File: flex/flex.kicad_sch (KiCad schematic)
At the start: 105 parts, among them J1 Conn_01x06_Female, J2 Conn_01x05_Female, J3 Conn_01x06_Female, J4 Conn_01x03_Female, J5 Conn_01x03_Female, SW1 SW_Push, SW10 SW_Push, SW11 SW_Push, SW12 SW_Push, SW13 SW_Push, SW14 SW_Push, SW15 SW_Push, SW16 SW_Push, SW17 SW_Push, SW18 SW_Push, SW19 SW_Push, SW2 SW_Push, SW20 SW_Push, SW21 SW_Push, SW22 SW_Push, SW23 SW_Push, SW24 SW_Push, SW3 SW_Push, SW4 SW_Push, SW5 SW_Push, SW6 SW_Push, SW7 SW_Push, SW8 SW_Push, SW9 SW_Push

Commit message: footprints
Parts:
- D1, D10, D11, D12, D2, D25, D26, D27, D28, D29, D3, D30, D31, D32, D33, D34, D35, D36, D4, D5, D6, D7, D8, D9: footprint libs:D_0402 -> libs:D_SOD-523
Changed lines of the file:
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@@
       (effects (font (size 1.27 1.27)) (justify right))
     )
-    (property "Footprint" "libs:D_0402" (at 66.04 44.45 0)
+    (property "Footprint" "libs:D_SOD-523" (at 66.04 44.45 0)
       (effects (font (size 1.27 1.27)) hide)
     )
@@
       (effects (font (size 1.27 1.27)) (justify right))
     )
-    (property "Footprint" "libs:D_0402" (at 226.06 57.15 0)
+    (property "Footprint" "libs:D_SOD-523" (at 226.06 57.15 0)
       (effects (font (size 1.27 1.27)) hide)
     )
@@
       (effects (font (size 1.27 1.27)) (justify right))
     )
-    (property "Footprint" "libs:D_0402" (at 226.06 80.01 0)
+    (property "Footprint" "libs:D_SOD-523" (at 226.06 80.01 0)
       (effects (font (size 1.27 1.27)) hide)
     )
@@
       (effects (font (size 1.27 1.27)) (justify right))
     )
-    (property "Footprint" "libs:D_0402" (at 330.2 57.15 0)
+    (property "Footprint" "libs:D_SOD-523" (at 330.2 57.15 0)
       (effects (font (size 1.27 1.27)) hide)
     )
@@
       (effects (font (size 1.27 1.27)) (justify right))
     )
-    (property "Footprint" "libs:D_0402" (at 176.53 80.01 0)
+    (property "Footprint" "libs:D_SOD-523" (at 176.53 80.01 0)
       (effects (font (size 1.27 1.27)) hide)
     )
@@
       (effects (font (size 1.27 1.27)) (justify right))
     )
-    (property "Footprint" "libs:D_0402" (at 176.53 57.15 0)
+    (property "Footprint" "libs:D_SOD-523" (at 176.53 57.15 0)
       (effects (font (size 1.27 1.27)) hide)
     )
@@
       (effects (font (size 1.27 1.27)) (justify right))
     )
-    (property "Footprint" "libs:D_0402" (at 279.4 93.98 0)
+    (property "Footprint" "libs:D_SOD-523" (at 279.4 93.98 0)
       (effects (font (size 1.27 1.27)) hide)
     )
@@
       (effects (font (size 1.27 1.27)) (justify right))
     )
-    (property "Footprint" "libs:D_0402" (at 118.11 93.98 0)
+    (property "Footprint" "libs:D_SOD-523" (at 118.11 93.98 0)
       (effects (font (size 1.27 1.27)) hide)
     )
@@
       (effects (font (size 1.27 1.27)) (justify right))
     )
-    (property "Footprint" "libs:D_0402" (at 276.86 57.15 0)
+    (property "Footprint" "libs:D_SOD-523" (at 276.86 57.15 0)
       (effects (font (size 1.27 1.27)) hide)
     )
@@
       (effects (font (size 1.27 1.27)) (justify right))
     )
-    (property "Footprint" "libs:D_0402" (at 66.04 93.98 0)
+    (property "Footprint" "libs:D_SOD-523" (at 66.04 93.98 0)
       (effects (font (size 1.27 1.27)) hide)
     )
@@
       (effects (font (size 1.27 1.27)) (justify right))
     )
-    (property "Footprint" "libs:D_0402" (at 116.84 44.45 0)
+    (property "Footprint" "libs:D_SOD-523" (at 116.84 44.45 0)
       (effects (font (size 1.27 1.27)) hide)
     )
@@
       (effects (font (size 1.27 1.27)) (justify right))
     )
-    (property "Footprint" "libs:D_0402" (at 226.06 93.98 0)
+    (property "Footprint" "libs:D_SOD-523" (at 226.06 93.98 0)
       (effects (font (size 1.27 1.27)) hide)
     )
@@
       (effects (font (size 1.27 1.27)) (justify right))
     )
-    (property "Footprint" "libs:D_0402" (at 226.06 43.18 0)
+    (property "Footprint" "libs:D_SOD-523" (at 226.06 43.18 0)
       (effects (font (size 1.27 1.27)) hide)
     )
@@
       (effects (font (size 1.27 1.27)) (justify right))
     )
-    (property "Footprint" "libs:D_0402" (at 330.2 80.01 0)
+    (property "Footprint" "libs:D_SOD-523" (at 330.2 80.01 0)
       (effects (font (size 1.27 1.27)) hide)
     )
@@
       (effects (font (size 1.27 1.27)) (justify right))
     )
-    (property "Footprint" "libs:D_0402" (at 279.4 80.01 0)
+    (property "Footprint" "libs:D_SOD-523" (at 279.4 80.01 0)
       (effects (font (size 1.27 1.27)) hide)
     )
@@
       (effects (font (size 1.27 1.27)) (justify right))
     )
-    (property "Footprint" "libs:D_0402" (at 116.84 58.42 0)
+    (property "Footprint" "libs:D_SOD-523" (at 116.84 58.42 0)
       (effects (font (size 1.27 1.27)) hide)
     )
@@
       (effects (font (size 1.27 1.27)) (justify right))
     )
-    (property "Footprint" "libs:D_0402" (at 118.11 80.01 0)
+    (property "Footprint" "libs:D_SOD-523" (at 118.11 80.01 0)
       (effects (font (size 1.27 1.27)) hide)
     )
@@
       (effects (font (size 1.27 1.27)) (justify right))
     )
-    (property "Footprint" "libs:D_0402" (at 176.53 43.18 0)
+    (property "Footprint" "libs:D_SOD-523" (at 176.53 43.18 0)
       (effects (font (size 1.27 1.27)) hide)
     )
@@
       (effects (font (size 1.27 1.27)) (justify right))
     )
-    (property "Footprint" "libs:D_0402" (at 330.2 43.18 0)
+    (property "Footprint" "libs:D_SOD-523" (at 330.2 43.18 0)
       (effects (font (size 1.27 1.27)) hide)
     )
@@
       (effects (font (size 1.27 1.27)) (justify right))
     )
-    (property "Footprint" "libs:D_0402" (at 66.04 80.01 0)
+    (property "Footprint" "libs:D_SOD-523" (at 66.04 80.01 0)
       (effects (font (size 1.27 1.27)) hide)
     )
@@
       (effects (font (size 1.27 1.27)) (justify right))
     )
-    (property "Footprint" "libs:D_0402" (at 330.2 93.98 0)
+    (property "Footprint" "libs:D_SOD-523" (at 330.2 93.98 0)
       (effects (font (size 1.27 1.27)) hide)
     )
@@
       (effects (font (size 1.27 1.27)) (justify right))
     )
-    (property "Footprint" "libs:D_0402" (at 66.04 58.42 0)
+    (property "Footprint" "libs:D_SOD-523" (at 66.04 58.42 0)
       (effects (font (size 1.27 1.27)) hide)
     )
@@
       (effects (font (size 1.27 1.27)) (justify right))
     )
-    (property "Footprint" "libs:D_0402" (at 276.86 43.18 0)
+    (property "Footprint" "libs:D_SOD-523" (at 276.86 43.18 0)
       (effects (font (size 1.27 1.27)) hide)
     )
@@
       (effects (font (size 1.27 1.27)) (justify right))
     )
-    (property "Footprint" "libs:D_0402" (at 176.53 93.98 0)
-      (effects (font (size 1.27 1.27)) hide)
-    )
+    (property "Footprint" "libs:D_SOD-523" (at 176.53 93.98 0)
+      (effects (font (size 1.27 1.27)) hide)
+    )

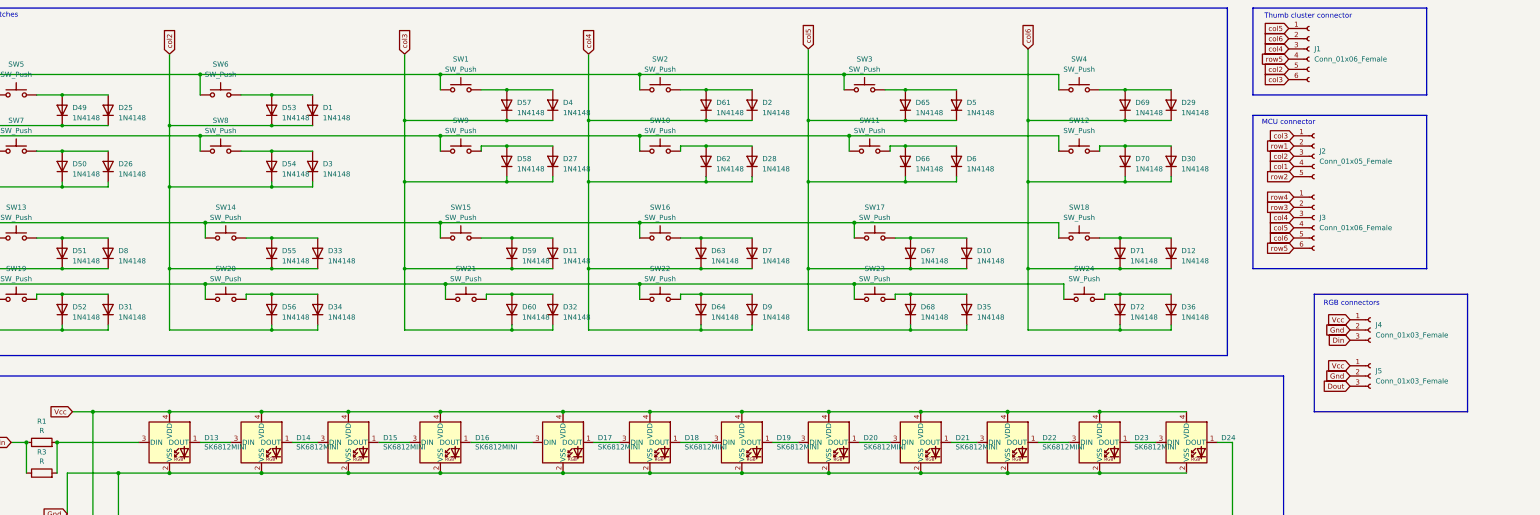
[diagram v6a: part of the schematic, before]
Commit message: separate into right/left diodes
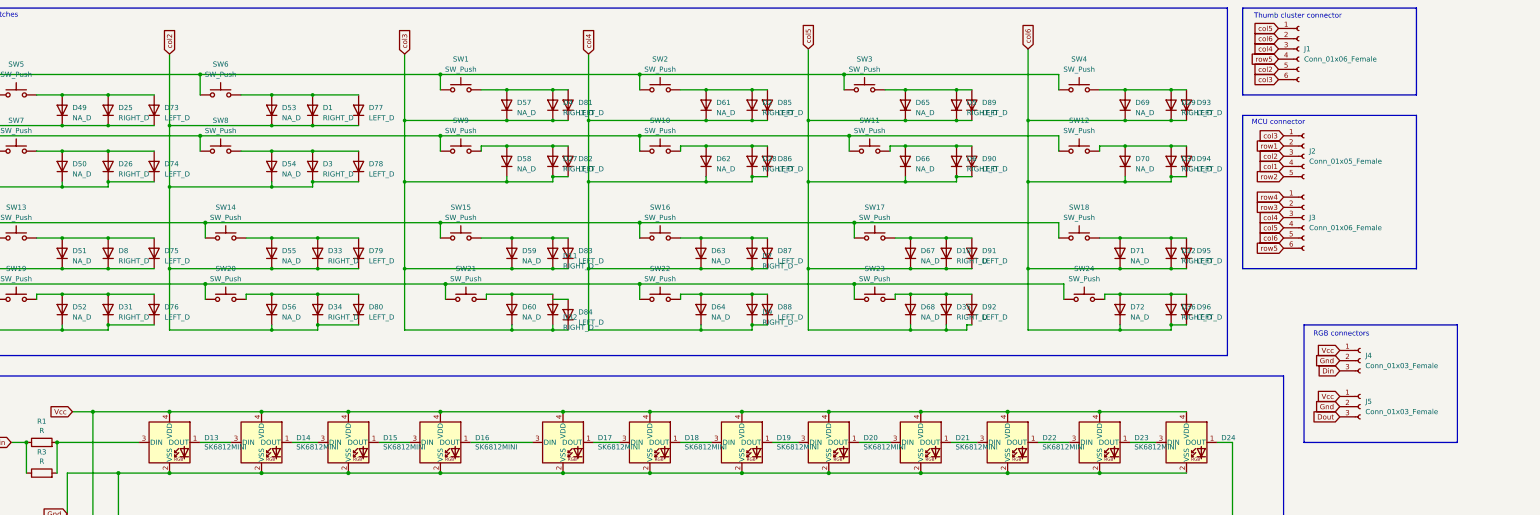
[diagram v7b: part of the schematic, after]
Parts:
- added D73, D74, D75, D76, D77, D78, D79, D80, D81, D82, D83, D84, D85, D86, D87, D88, D89, D90, D91, D92, D93, D94, D95, D96: LEFT_D, libs:D_SOD-523, symbol Diode:1N4148
- D1, D10, D11, D12, D2, D25, D26, D27, D28, D29, D3, D30, D31, D32, D33, D34, D35, D36, D4, D5, D6, D7, D8, D9: value 1N4148 -> RIGHT_D
- D49, D50, D51, D52, D53, D54, D55, D56, D57, D58, D59, D60, D61, D62, D63, D64, D65, D66, D67, D68, D69, D70, D71, D72: value 1N4148 -> NA_D
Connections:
- net col1: now also D73.1 (K), D74.1 (K), D75.1 (K), D76.1 (K)
- net col2: now also D77.1 (K), D78.1 (K), D79.1 (K), D80.1 (K)
- net col3: now also D81.1 (K), D82.1 (K), D83.1 (K), D84.1 (K)
- net col4: now also D85.1 (K), D86.1 (K), D87.1 (K), D88.1 (K)
- net col5: now also D89.1 (K), D90.1 (K), D91.1 (K), D92.1 (K)
- net col6: now also D93.1 (K), D94.1 (K), D95.1 (K), D96.1 (K)
- net at D26.2 (A), D50.2 (A), SW7.2: now also D74.2 (A)
- net at D25.2 (A), D49.2 (A), SW5.2: now also D73.2 (A)
- net at D35.2 (A), D68.2 (A), SW23.2: now also D92.2 (A)
- net at D28.2 (A), D62.2 (A), SW10.2: now also D86.2 (A)
- net at D63.2 (A), D7.2 (A), SW16.2: now also D87.2 (A)
- net at D2.2 (A), D61.2 (A), SW2.2: now also D85.2 (A)
- net at D30.2 (A), D70.2 (A), SW12.2: now also D94.2 (A)
- net at D11.2 (A), D59.2 (A), SW15.2: now also D83.2 (A)
- net at D27.2 (A), D58.2 (A), SW9.2: now also D82.2 (A)
- net at D1.2 (A), D53.2 (A), SW6.2: now also D77.2 (A)
- net at D34.2 (A), D56.2 (A), SW20.2: now also D80.2 (A)
- net at D6.2 (A), D66.2 (A), SW11.2: now also D90.2 (A)
- net at D33.2 (A), D55.2 (A), SW14.2: now also D79.2 (A)
- net at D10.2 (A), D67.2 (A), SW17.2: now also D91.2 (A)
- net at D3.2 (A), D54.2 (A), SW8.2: now also D78.2 (A)
- net at D51.2 (A), D8.2 (A), SW13.2: now also D75.2 (A)
- net at D31.2 (A), D52.2 (A), SW19.2: now also D76.2 (A)
- net at D64.2 (A), D9.2 (A), SW22.2: now also D88.2 (A)
- net at D12.2 (A), D71.2 (A), SW18.2: now also D95.2 (A)
- net at D4.2 (A), D57.2 (A), SW1.2: now also D81.2 (A)
- net at D5.2 (A), D65.2 (A), SW3.2: now also D89.2 (A)
- net at D29.2 (A), D69.2 (A), SW4.2: now also D93.2 (A)
- net at D36.2 (A), D72.2 (A), SW24.2: now also D96.2 (A)
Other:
- moved on the sheet: D10, D35, J1, J2, J3, J4, J5

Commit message: left/right capacitor resistor
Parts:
- added C2: LEFT_C, libs:D_0402, symbol Device:C
- added R2: LEFT_R, libs:D_0402, symbol Device:R
- C1: value C -> RIGHT_C
- C3: value C3 -> NA_C
- J1, J3: value Conn_01x06_Female -> NA_Conn_01x06_Female
- J2: value Conn_01x05_Female -> NA_Conn_01x05_Female
- J4, J5: value Conn_01x03_Female -> NA_Conn_01x03_Female
- R1: value R -> RIGHT_R
- R3: value R -> NA_R
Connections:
- net Din: now also R2.1
- net Gnd: now also C2.2
- net Vcc: now also C2.1
- net at D13.3 (DIN), R1.2, R3.2: now also R2.2
- net at D32.2 (A), D60.2 (A), SW21.2: now also D84.2 (A)
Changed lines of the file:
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@@
   (junction (at 66.04 76.2) (diameter 0) (color 0 0 0 0)
   )
+  (junction (at 176.53 90.17) (diameter 0) (color 0 0 0 0)
+  )
   (junction (at 330.2 53.34) (diameter 0) (color 0 0 0 0)
   )
@@
   (junction (at 176.53 39.37) (diameter 0) (color 0 0 0 0)
   )
+  (junction (at 48.26 182.88) (diameter 0) (color 0 0 0 0)
+  )
   (junction (at 165.1 53.34) (diameter 0) (color 0 0 0 0)
   )
@@
   (junction (at 148.59 134.62) (diameter 1.016) (color 0 0 0 0)
   )
+  (junction (at 45.72 130.81) (diameter 0) (color 0 0 0 0)
+  )
   (junction (at 82.55 166.37) (diameter 1.016) (color 0 0 0 0)
   )
@@
   (junction (at 214.63 46.99) (diameter 0) (color 0 0 0 0)
   )
+  (junction (at 48.26 175.26) (diameter 0) (color 0 0 0 0)
+  )
   (junction (at 245.11 134.62) (diameter 1.016) (color 0 0 0 0)
   )
@@
   (junction (at 127 181.61) (diameter 1.016) (color 0 0 0 0)
   )
+  (junction (at 53.34 130.81) (diameter 0) (color 0 0 0 0)
+  )
   (junction (at 260.35 181.61) (diameter 1.016) (color 0 0 0 0)
   )
@@
     (stroke (width 0) (type solid))
   )
+  (wire (pts (xy 53.34 130.81) (xy 53.34 134.62))
+    (stroke (width 0) (type solid))
+  )
   (wire (pts (xy 81.28 63.5) (xy 81.28 83.82))
     (stroke (width 0) (type solid))
@@
     (stroke (width 0) (type solid))
   )
+  (wire (pts (xy 180.34 91.44) (xy 176.53 91.44))
+    (stroke (width 0) (type default))
+  )
   (wire (pts (xy 198.12 87.63) (xy 198.12 91.44))
     (stroke (width 0) (type solid))
@@
     (stroke (width 0) (type default))
   )
+  (wire (pts (xy 48.26 175.26) (xy 52.07 175.26))
+    (stroke (width 0) (type default))
+  )
   (wire (pts (xy 276.86 60.96) (xy 280.67 60.96))
     (stroke (width 0) (type default))
@@
     (stroke (width 0) (type solid))
   )
-  (wire (pts (xy 45.72 175.26) (xy 52.07 175.26))
+  (wire (pts (xy 45.72 175.26) (xy 48.26 175.26))
     (stroke (width 0) (type default))
   )
@@
     (stroke (width 0) (type solid))
   )
-  (wire (pts (xy 45.72 182.88) (xy 52.07 182.88))
+  (wire (pts (xy 45.72 182.88) (xy 48.26 182.88))
     (stroke (width 0) (type default))
   )
@@
     (stroke (width 0) (type solid))
   )
+  (wire (pts (xy 48.26 182.88) (xy 52.07 182.88))
+    (stroke (width 0) (type default))
+  )
   (wire (pts (xy 35.56 50.8) (xy 38.1 50.8))
     (stroke (width 0) (type solid))
@@
     (stroke (width 0) (type default))
   )
-  (wire (pts (xy 45.72 127) (xy 45.72 134.62))
+  (wire (pts (xy 45.72 127) (xy 45.72 130.81))
     (stroke (width 0) (type default))
   )
@@
     (stroke (width 0) (type solid))
   )
+  (wire (pts (xy 45.72 130.81) (xy 45.72 134.62))
+    (stroke (width 0) (type default))
+  )
   (polyline (pts (xy 347.98 45.72) (xy 347.98 83.82))
     (stroke (width 0) (type default))
@@
     (stroke (width 0) (type solid))
   )
-  (wire (pts (xy 53.34 127) (xy 53.34 134.62))
+  (wire (pts (xy 53.34 127) (xy 53.34 130.81))
     (stroke (width 0) (type solid))
   )
@@
     (stroke (width 0) (type solid))
   )
+  (wire (pts (xy 176.53 91.44) (xy 176.53 90.17))
+    (stroke (width 0) (type default))
+  )
   (wire (pts (xy 171.45 166.37) (xy 193.04 166.37))
     (stroke (width 0) (type solid))
@@
     (stroke (width 0) (type solid))
   )
-  (wire (pts (xy 176.53 91.44) (xy 180.34 91.44))
-    (stroke (width 0) (type solid))
-  )
   (wire (pts (xy 223.52 119.38) (xy 245.11 119.38))
     (stroke (width 0) (type solid))
@@
     )
   )
+  (symbol (lib_id "Device:R") (at 49.53 130.81 90) (unit 1)
+    (in_bom yes) (on_board yes) (dnp no)
+    (property "Reference" "R2" (at 49.53 125.5838 90)
+      (effects (font (size 1.27 1.27)))
+    )
+    (property "Value" "LEFT_R" (at 49.53 127.8825 90)
+      (effects (font (size 1.27 1.27)))
+    )
+    (property "Footprint" "libs:D_0402" (at 49.53 132.588 90)
+      (effects (font (size 1.27 1.27)) hide)
+    )
+    (property "Datasheet" "~" (at 49.53 130.81 0)
+      (effects (font (size 1.27 1.27)) hide)
+    )
+    (pin "1")
+    (pin "2")
+    (instances
+      (project "flex"
+        (path "/e63e39d7-6ac0-4ffd-8aa3-1841a4541b55"
+          (reference "R2") (unit 1)
+        )
+      )
+    )
+  )
   (symbol (lib_id "Device:C") (at 38.1 179.07 0) (unit 1)
     (in_bom yes) (on_board yes) (dnp no)
@@
       (effects (font (size 1.27 1.27)) (justify left))
     )
-    (property "Value" "C" (at 41.0211 180.2193 0)
+    (property "Value" "RIGHT_C" (at 41.0211 180.2193 0)
       (effects (font (size 1.27 1.27)) (justify left))
     )
@@
       (effects (font (size 1.27 1.27)) (justify left))
     )
-    (property "Value" "Conn_01x03_Female" (at 378.46 119.38 0)
+    (property "Value" "NA_Conn_01x03_Female" (at 378.46 119.38 0)
       (effects (font (size 1.27 1.27)) (justify left))
     )
@@
     )
   )
+  (symbol (lib_id "Device:C") (at 48.26 179.07 0) (unit 1)
+    (in_bom yes) (on_board yes) (dnp no)
+    (property "Reference" "C2" (at 51.1811 177.9206 0)
+      (effects (font (size 1.27 1.27)) (justify left))
+    )
+    (property "Value" "LEFT_C" (at 51.1811 180.2193 0)
+      (effects (font (size 1.27 1.27)) (justify left))
+    )
+    (property "Footprint" "libs:D_0402" (at 49.2252 182.88 0)
+      (effects (font (size 1.27 1.27)) hide)
+    )
+    (property "Datasheet" "~" (at 48.26 179.07 0)
+      (effects (font (size 1.27 1.27)) hide)
+    )
+    (pin "1")
+    (pin "2")
+    (instances
+      (project "flex"
+        (path "/e63e39d7-6ac0-4ffd-8aa3-1841a4541b55"
+          (reference "C2") (unit 1)
+        )
+      )
+    )
+  )
   (symbol (lib_id "Switch:SW_Push") (at 93.98 54.61 0) (unit 1)
     (in_bom no) (on_board yes) (dnp no)
@@
       (effects (font (size 1.27 1.27)) (justify left))
     )
-    (property "Value" "Conn_01x03_Female" (at 378.46 107.95 0)
+    (property "Value" "NA_Conn_01x03_Female" (at 378.46 107.95 0)
       (effects (font (size 1.27 1.27)) (justify left))
     )
@@
       (effects (font (size 1.27 1.27)) (justify left))
     )
-    (property "Value" "Conn_01x05_Female" (at 364.49 57.15 0)
+    (property "Value" "NA_Conn_01x05_Female" (at 364.49 57.15 0)
       (effects (font (size 1.27 1.27)) (justify left))
     )
@@
       (effects (font (size 1.27 1.27)))
     )
-    (property "Value" "R" (at 49.53 124.0725 90)
+    (property "Value" "RIGHT_R" (at 49.53 124.0725 90)
       (effects (font (size 1.27 1.27)))
     )
@@
       (effects (font (size 1.27 1.27)))
     )
-    (property "Value" "R" (at 49.53 131.6925 90)
+    (property "Value" "NA_R" (at 49.53 131.6925 90)
       (effects (font (size 1.27 1.27)))
     )
@@
       (effects (font (size 1.27 1.27)) (justify left) hide)
     )
-    (property "Value" "C3" (at 54.9911 180.2193 0)
+    (property "Value" "NA_C" (at 54.9911 180.2193 0)
       (effects (font (size 1.27 1.27)) (justify left))
     )
@@
       (effects (font (size 1.27 1.27)) (justify left))
     )
-    (property "Value" "Conn_01x06_Female" (at 364.49 73.66 0)
+    (property "Value" "NA_Conn_01x06_Female" (at 364.49 73.66 0)
       (effects (font (size 1.27 1.27)) (justify left))
     )
@@
       (effects (font (size 1.27 1.27)) (justify left))
     )
-    (property "Value" "Conn_01x06_Female" (at 363.22 31.75 0)
+    (property "Value" "NA_Conn_01x06_Female" (at 363.22 31.75 0)
       (effects (font (size 1.27 1.27)) (justify left))
     )
